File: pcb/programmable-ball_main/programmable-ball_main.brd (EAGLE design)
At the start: 30.5 x 30.8 mm, 1 part, among them U1 MDBT50Q-1MV2

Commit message: 軽微な修正 #4
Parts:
- moved U1 3.32 mm to (15.0, 19.0)
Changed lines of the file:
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@@
 </autorouter>
 <elements>
-<element name="U1" library="MDBT50Q-1MV2" package="XCVR_MDBT50Q-1MV2" value="MDBT50Q-1MV2" x="15.13" y="22.32" smashed="yes">
-<attribute name="AVAILABILITY" value="In Stock" x="15.13" y="22.32" size="1.778" layer="27" display="off"/>
-<attribute name="CHECK_PRICES" value="https://www.snapeda.com/parts/MDBT50Q-1MV2/Raytac+Corporation/view-part/?ref=eda" x="15.13" y="22.32" size="1.778" layer="27" display="off"/>
-<attribute name="DESCRIPTION" value=" 802.15.4, Bluetooth Bluetooth v5.2, Zigbee® Transceiver Module 2.36GHz ~ 2.5GHz Integrated, Chip Surface Mount " x="15.13" y="22.32" size="1.778" layer="27" display="off"/>
-<attribute name="MF" value="Raytac Corporation" x="15.13" y="22.32" size="1.778" layer="27" display="off"/>
-<attribute name="MP" value="MDBT50Q-1MV2" x="15.13" y="22.32" size="1.778" layer="27" display="off"/>
-<attribute name="NAME" x="6.88" y="24.51" size="1.27" layer="25"/>
-<attribute name="PACKAGE" value="SMD-61 Raytac Corporation" x="15.13" y="22.32" size="1.778" layer="27" display="off"/>
-<attribute name="PRICE" value="None" x="15.13" y="22.32" size="1.778" layer="27" display="off"/>
-<attribute name="SNAPEDA_LINK" value="https://www.snapeda.com/parts/MDBT50Q-1MV2/Raytac+Corporation/view-part/?ref=snap" x="15.13" y="22.32" size="1.778" layer="27" display="off"/>
-<attribute name="VALUE" x="8.51" y="12.87" size="1.27" layer="27"/>
+<element name="U1" library="MDBT50Q-1MV2" package="XCVR_MDBT50Q-1MV2" value="MDBT50Q-1MV2" x="15" y="19" smashed="yes">
+<attribute name="AVAILABILITY" value="In Stock" x="15" y="19" size="1.778" layer="27" display="off"/>
+<attribute name="CHECK_PRICES" value="https://www.snapeda.com/parts/MDBT50Q-1MV2/Raytac+Corporation/view-part/?ref=eda" x="15" y="19" size="1.778" layer="27" display="off"/>
+<attribute name="DESCRIPTION" value=" 802.15.4, Bluetooth Bluetooth v5.2, Zigbee® Transceiver Module 2.36GHz ~ 2.5GHz Integrated, Chip Surface Mount " x="15" y="19" size="1.778" layer="27" display="off"/>
+<attribute name="MF" value="Raytac Corporation" x="15" y="19" size="1.778" layer="27" display="off"/>
+<attribute name="MP" value="MDBT50Q-1MV2" x="15" y="19" size="1.778" layer="27" display="off"/>
+<attribute name="NAME" x="9.75" y="27.19" size="1.27" layer="25"/>
+<attribute name="PACKAGE" value="SMD-61 Raytac Corporation" x="15" y="19" size="1.778" layer="27" display="off"/>
+<attribute name="PRICE" value="None" x="15" y="19" size="1.778" layer="27" display="off"/>
+<attribute name="SNAPEDA_LINK" value="https://www.snapeda.com/parts/MDBT50Q-1MV2/Raytac+Corporation/view-part/?ref=snap" x="15" y="19" size="1.778" layer="27" display="off"/>
+<attribute name="VALUE" x="9.65" y="9.55" size="1.27" layer="27"/>
 </element>
 </elements>
 <signals>
 <signal name="GND">
+<contactref element="U1" pad="55"/>
+<contactref element="U1" pad="1"/>
+<contactref element="U1" pad="15"/>
 <contactref element="U1" pad="33"/>
-<contactref element="U1" pad="1"/>
 <contactref element="U1" pad="2"/>
-<contactref element="U1" pad="15"/>
-<contactref element="U1" pad="55"/>
-<wire x1="10.48" y1="26.07" x2="19.78" y2="26.07" width="0" layer="19" extent="1-1"/>
-<wire x1="10.48" y1="24.97" x2="10.48" y2="26.07" width="0" layer="19" extent="1-1"/>
-<wire x1="10.33" y1="15.17" x2="10.48" y2="24.97" width="0" layer="19" extent="1-1"/>
-<wire x1="19.93" y1="15.17" x2="10.33" y2="15.17" width="0" layer="19" extent="1-1"/>
+<wire x1="19.8" y1="11.85" x2="10.2" y2="11.85" width="0" layer="19" extent="1-1"/>
+<wire x1="10.35" y1="21.65" x2="10.2" y2="11.85" width="0" layer="19" extent="1-1"/>
+<wire x1="10.35" y1="22.75" x2="10.35" y2="21.65" width="0" layer="19" extent="1-1"/>
+<wire x1="19.65" y1="22.75" x2="10.35" y2="22.75" width="0" layer="19" extent="1-1"/>
 </signal>
 <signal name="VDDH">

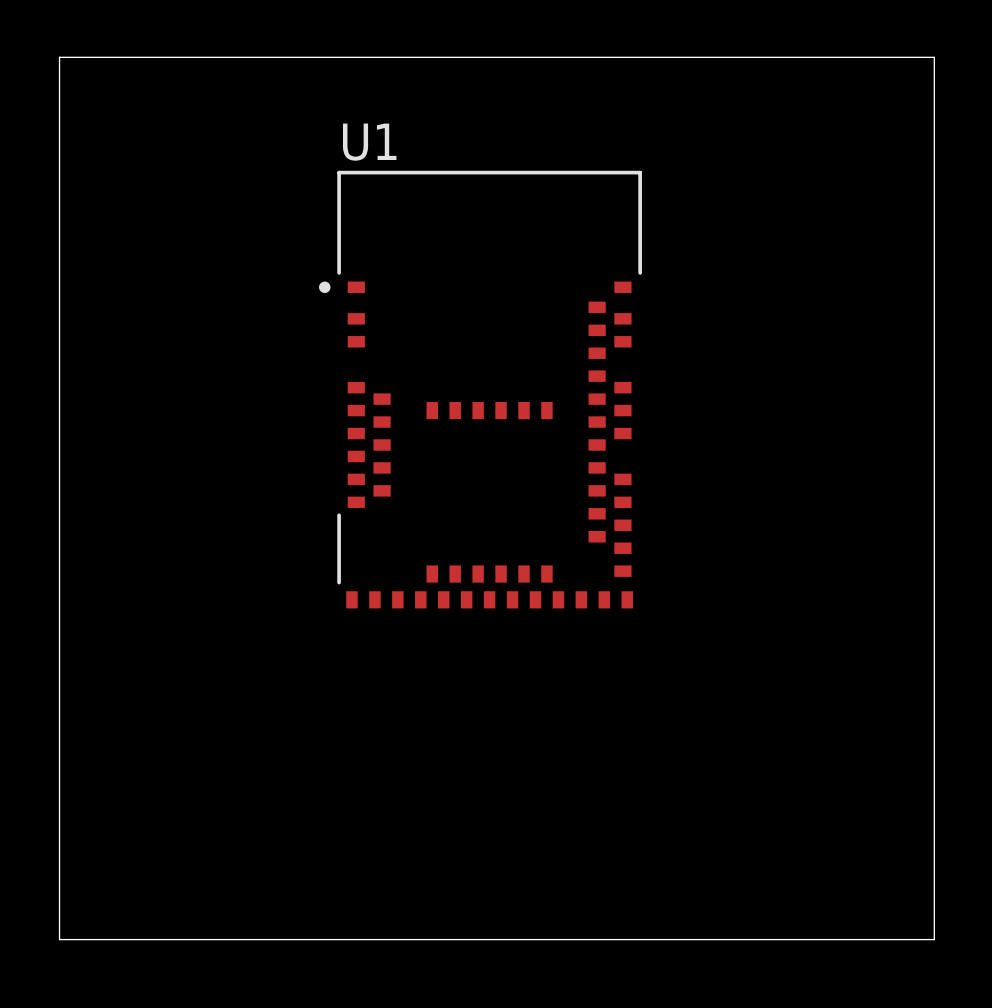
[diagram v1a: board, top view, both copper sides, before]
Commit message: Added Circular Board and TypeC Connector #4
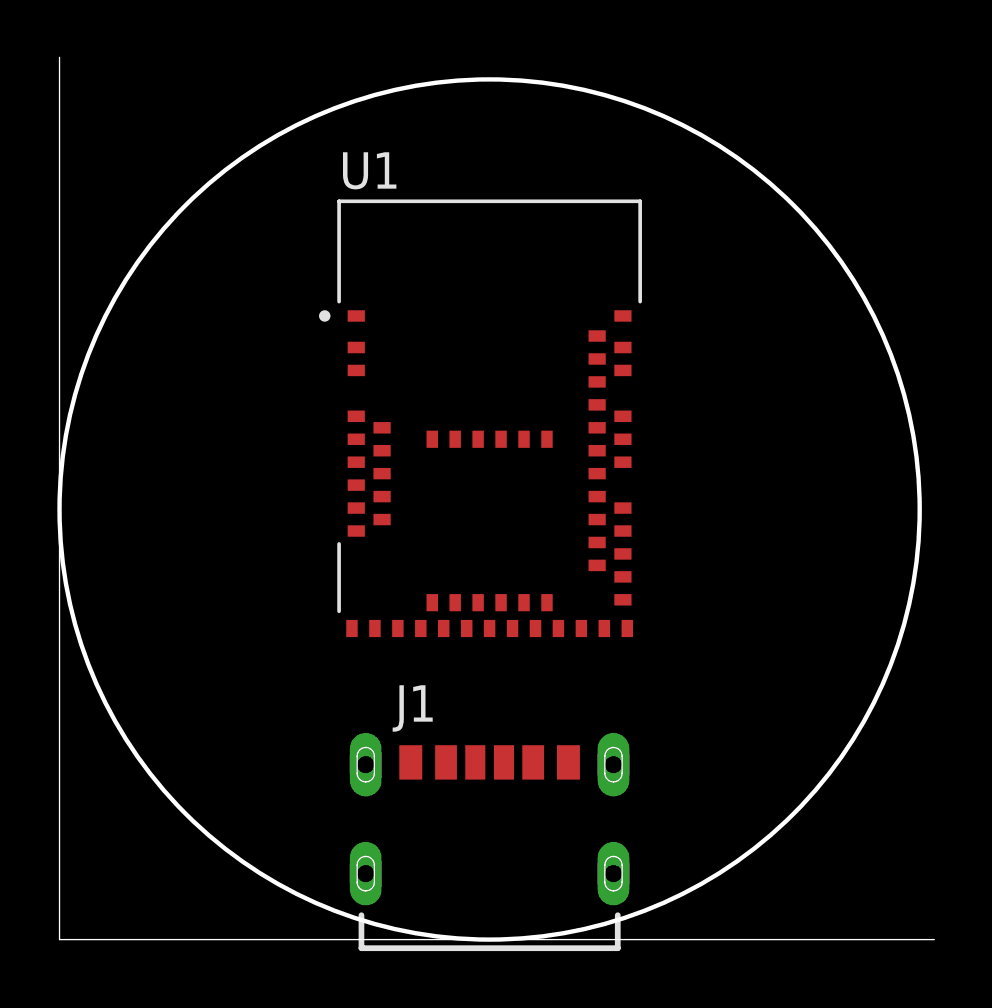
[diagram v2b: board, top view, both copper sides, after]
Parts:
- added J1: USB4125-GF-A_REVA2, USB4125-GF-A_REVA2:GCT_USB4125-GF-A_REVA2
- moved U1 1.00 mm to (15.0, 18.0)
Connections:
- net GND: now also J1.A12, J1.B12
- net VBUS: now also J1.A9, J1.B9
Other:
- outline, holes or cut-outs redrawn
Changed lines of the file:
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@@
 <setting verticaltext="up"/>
 </settings>
-<grid distance="1" unitdist="mm" unit="mm" style="lines" multiple="1" display="yes" altdistance="5" altunitdist="mil" altunit="mil"/>
+<grid distance="1" unitdist="mm" unit="mm" style="lines" multiple="1" display="yes" altdistance="0.1" altunitdist="mm" altunit="mm"/>
 <layers>
 <layer number="1" name="Top" color="4" fill="1" visible="yes" active="yes"/>
@@
 <plain>
 <wire x1="0" y1="0" x2="30.51" y2="0" width="0" layer="20"/>
-<wire x1="30.51" y1="0" x2="30.51" y2="30.77" width="0" layer="20"/>
-<wire x1="30.51" y1="30.77" x2="0" y2="30.77" width="0" layer="20"/>
 <wire x1="0" y1="30.77" x2="0" y2="0" width="0" layer="20"/>
 <dimension x1="0" y1="0" x2="0" y2="30" x3="-6" y3="15" textsize="1.778" layer="47"/>
 <dimension x1="0" y1="0" x2="30" y2="0" x3="15" y3="-6" textsize="1.778" layer="47"/>
+<circle x="15" y="15" radius="15" width="0.1524" layer="20"/>
 </plain>
 <attributes>
@@
 </autorouter>
 <elements>
-<element name="U1" library="MDBT50Q-1MV2" package="XCVR_MDBT50Q-1MV2" value="MDBT50Q-1MV2" x="15" y="19" smashed="yes">
-<attribute name="AVAILABILITY" value="In Stock" x="15" y="19" size="1.778" layer="27" display="off"/>
-<attribute name="CHECK_PRICES" value="https://www.snapeda.com/parts/MDBT50Q-1MV2/Raytac+Corporation/view-part/?ref=eda" x="15" y="19" size="1.778" layer="27" display="off"/>
-<attribute name="DESCRIPTION" value=" 802.15.4, Bluetooth Bluetooth v5.2, Zigbee® Transceiver Module 2.36GHz ~ 2.5GHz Integrated, Chip Surface Mount " x="15" y="19" size="1.778" layer="27" display="off"/>
-<attribute name="MF" value="Raytac Corporation" x="15" y="19" size="1.778" layer="27" display="off"/>
-<attribute name="MP" value="MDBT50Q-1MV2" x="15" y="19" size="1.778" layer="27" display="off"/>
-<attribute name="NAME" x="9.75" y="27.19" size="1.27" layer="25"/>
-<attribute name="PACKAGE" value="SMD-61 Raytac Corporation" x="15" y="19" size="1.778" layer="27" display="off"/>
-<attribute name="PRICE" value="None" x="15" y="19" size="1.778" layer="27" display="off"/>
-<attribute name="SNAPEDA_LINK" value="https://www.snapeda.com/parts/MDBT50Q-1MV2/Raytac+Corporation/view-part/?ref=snap" x="15" y="19" size="1.778" layer="27" display="off"/>
-<attribute name="VALUE" x="9.65" y="9.55" size="1.27" layer="27"/>
+<element name="U1" library="MDBT50Q-1MV2" package="XCVR_MDBT50Q-1MV2" value="MDBT50Q-1MV2" x="15" y="18" smashed="yes">
+<attribute name="AVAILABILITY" value="In Stock" x="15" y="18" size="1.778" layer="27" display="off"/>
+<attribute name="CHECK_PRICES" value="https://www.snapeda.com/parts/MDBT50Q-1MV2/Raytac+Corporation/view-part/?ref=eda" x="15" y="18" size="1.778" layer="27" display="off"/>
+<attribute name="DESCRIPTION" value=" 802.15.4, Bluetooth Bluetooth v5.2, Zigbee® Transceiver Module 2.36GHz ~ 2.5GHz Integrated, Chip Surface Mount " x="15" y="18" size="1.778" layer="27" display="off"/>
+<attribute name="MF" value="Raytac Corporation" x="15" y="18" size="1.778" layer="27" display="off"/>
+<attribute name="MP" value="MDBT50Q-1MV2" x="15" y="18" size="1.778" layer="27" display="off"/>
+<attribute name="NAME" x="9.75" y="26.19" size="1.27" layer="25"/>
+<attribute name="PACKAGE" value="SMD-61 Raytac Corporation" x="15" y="18" size="1.778" layer="27" display="off"/>
+<attribute name="PRICE" value="None" x="15" y="18" size="1.778" layer="27" display="off"/>
+<attribute name="SNAPEDA_LINK" value="https://www.snapeda.com/parts/MDBT50Q-1MV2/Raytac+Corporation/view-part/?ref=snap" x="15" y="18" size="1.778" layer="27" display="off"/>
+</element>
+<element name="J1" library="USB4125-GF-A_REVA2" package="GCT_USB4125-GF-A_REVA2" value="USB4125-GF-A_REVA2" x="15" y="3.1" smashed="yes">
+<attribute name="DESCRIPTION" value=" USB Charge Only Connector Type C Horizontal Receptacle, 3.16mm profile, 6 Pins, Surface mount, Top mount, low cost " x="15" y="3.1" size="1.778" layer="27" display="off"/>
+<attribute name="DIGI-KEY_PART_NUMBER" value="2073-USB4125-GF-ATR-ND" x="15" y="3.1" size="1.778" layer="27" display="off"/>
+<attribute name="MF" value="Global Connector Technology" x="15" y="3.1" size="1.778" layer="27" display="off"/>
+<attribute name="MP" value="USB4125-GF-A" x="15" y="3.1" size="1.778" layer="27" display="off"/>
+<attribute name="NAME" x="11.7" y="7.6" size="1.27" layer="25"/>
+<attribute name="PACKAGE" value="None" x="15" y="3.1" size="1.778" layer="27" display="off"/>
+<attribute name="PURCHASE-URL" value="https://pricing.snapeda.com/search/part/USB4125-GF-A/?ref=eda" x="15" y="3.1" size="1.778" layer="27" display="off"/>
 </element>
 </elements>
@@
 <contactref element="U1" pad="33"/>
 <contactref element="U1" pad="2"/>
-<wire x1="19.8" y1="11.85" x2="10.2" y2="11.85" width="0" layer="19" extent="1-1"/>
-<wire x1="10.35" y1="21.65" x2="10.2" y2="11.85" width="0" layer="19" extent="1-1"/>
-<wire x1="10.35" y1="22.75" x2="10.35" y2="21.65" width="0" layer="19" extent="1-1"/>
-<wire x1="19.65" y1="22.75" x2="10.35" y2="22.75" width="0" layer="19" extent="1-1"/>
+<contactref element="J1" pad="B12"/>
+<contactref element="J1" pad="A12"/>
+<wire x1="10.35" y1="21.75" x2="19.65" y2="21.75" width="0" layer="19" extent="1-1"/>
+<wire x1="10.35" y1="20.65" x2="10.35" y2="21.75" width="0" layer="19" extent="1-1"/>
+<wire x1="10.2" y1="10.85" x2="10.35" y2="20.65" width="0" layer="19" extent="1-1"/>
+<wire x1="19.8" y1="10.85" x2="10.2" y2="10.85" width="0" layer="19" extent="1-1"/>
+<wire x1="17.75" y1="6.18" x2="10.2" y2="10.85" width="0" layer="19" extent="1-1"/>
+<wire x1="12.25" y1="6.18" x2="17.75" y2="6.18" width="0" layer="19" extent="1-1"/>
 </signal>
 <signal name="VDDH">
@@
 <signal name="VBUS">
 <contactref element="U1" pad="32"/>
+<contactref element="J1" pad="B9"/>
+<contactref element="J1" pad="A9"/>
+<wire x1="16.52" y1="6.18" x2="19" y2="10.85" width="0" layer="19" extent="1-1"/>
+<wire x1="13.48" y1="6.18" x2="16.52" y2="6.18" width="0" layer="19" extent="1-1"/>
 </signal>
 <signal name="DCCH">
